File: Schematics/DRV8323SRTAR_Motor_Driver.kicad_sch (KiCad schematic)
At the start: 20 parts, among them U6 DRV8323SRTAR

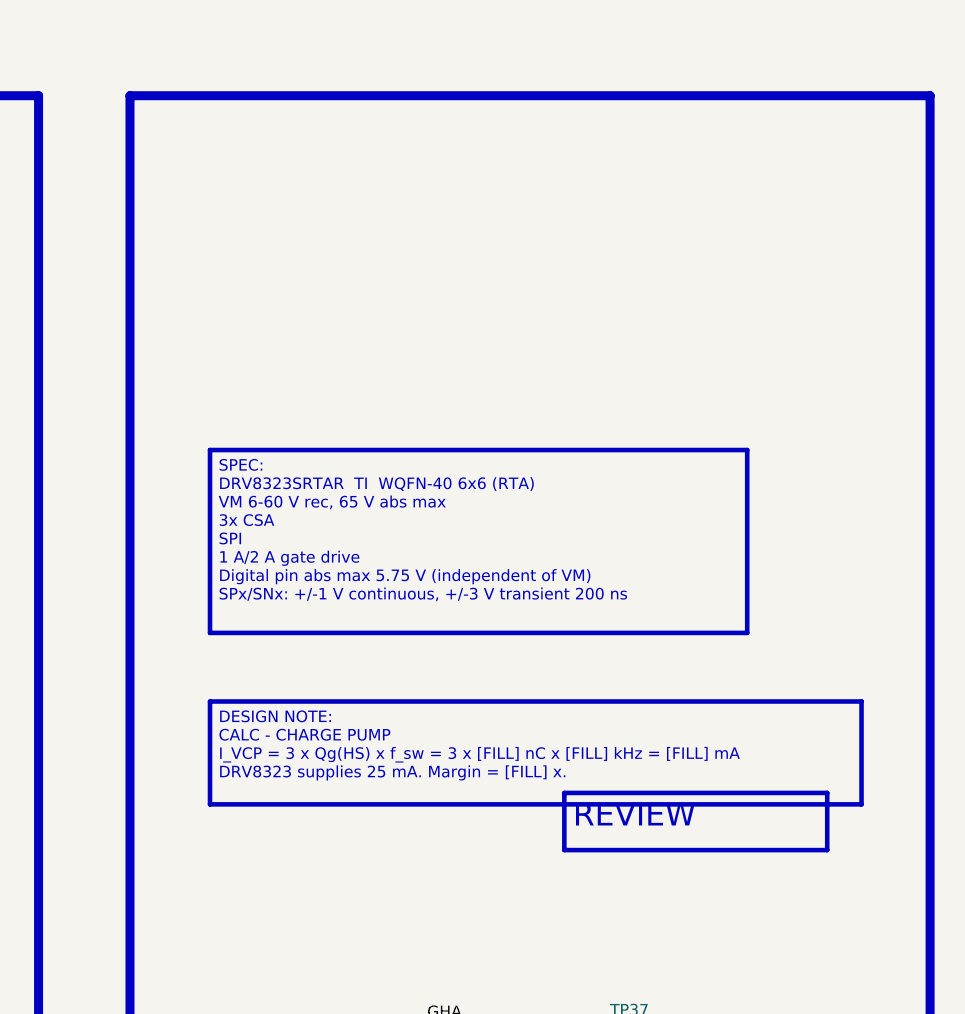
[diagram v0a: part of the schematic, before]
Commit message: Clean up schematic design notes; export schematic and PCB artwork PDFs
- Remove firmware-only notes (boot sequence, calibration procedure,
  firmware SPI/PWM settings) and template/empty text; keep hardware facts
- Tighten wording of all DESIGN/SPEC/ASSEMBLY/REV 1 notes and resize
  boxes so no note text wraps or overflows
- Re-export schematic PDF
- Add PCB artwork PDFs (combined and one per layer: silk, paste, mask,
  L1-L6 copper), board outline on every page

Co-Authored-By: Claude Opus 5.5 <noreply@anthropic.com>
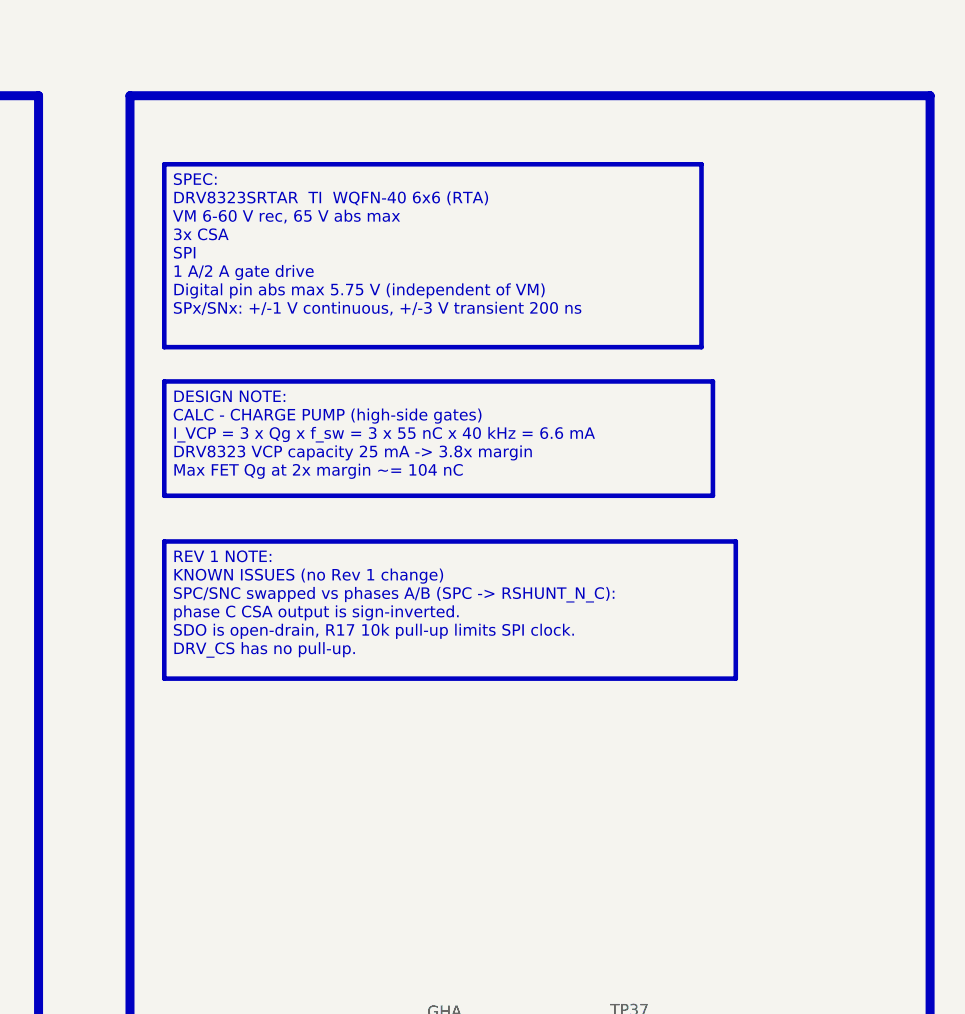
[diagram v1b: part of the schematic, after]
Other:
- company: (none) -> ${COMPANY}
- title: (none) -> Motor Control - Driver
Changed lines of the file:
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@@
 	(generator_version "10.0")
 	(paper "A3")
+	(title_block
+		(title "Motor Control - Driver")
+		(date "${RELEASE_DATE}")
+		(rev "${REVISION}")
+		(company "${COMPANY}")
+	)
 	(rectangle
 		(start 25.4 38.1)
@@
 		)
 	)
-	(text_box "REVIEW"
-		(exclude_from_sim no)
-		(at 350.52 115.57 0)
-		(size 29.21 6.35)
-		(margins 0.9525 0.9525 0.9525 0.9525)
-		(stroke
-			(width 0.508)
-			(type solid)
-			(color 255 0 0 1)
-		)
-		(fill
-			(type color)
-			(color 255 0 0 1)
-		)
-		(effects
-			(font
-				(size 2.54 2.54)
-				(color 0 0 0 1)
-			)
-			(justify left top)
-		)
-	)
 	(text_box "SPEC:\nDRV8323SRTAR  TI  WQFN-40 6x6 (RTA)\nVM 6-60 V rec, 65 V abs max \n3x CSA \nSPI\n1 A/2 A gate drive\nDigital pin abs max 5.75 V (independent of VM)\nSPx/SNx: +/-1 V continuous, +/-3 V transient 200 ns"
 		(exclude_from_sim no)
-		(at 311.15 77.4701 0)
+		(at 306.07 45.72 0)
 		(size 59.69 20.3199)
 		(margins 0.9525 0.9525 0.9525 0.9525)
@@
 		)
 	)
-	(text_box "DESIGN NOTE:\nCALC - CHARGE PUMP\nI_VCP = 3 x Qg(HS) x f_sw = 3 x [FILL] nC x [FILL] kHz = [FILL] mA\nDRV8323 supplies 25 mA. Margin = [FILL] x."
-		(exclude_from_sim no)
-		(at 311.15 105.4101 0)
-		(size 72.39 11.43)
-		(margins 0.9525 0.9525 0.9525 0.9525)
-		(stroke
-			(width 0.508)
-			(type solid)
-			(color 0 0 255 1)
-		)
-		(fill
-			(type color)
-			(color 255 255 255 1)
-		)
-		(effects
-			(font
-				(size 1.27 1.27)
-				(color 0 0 0 1)
-			)
-			(justify left top)
-		)
-	)
 	(text_box "Motor Driver\n"
 		(exclude_from_sim no)
@@
 		)
 	)
-)
+	(text_box "DESIGN NOTE:\nCALC - CHARGE PUMP (high-side gates)\nI_VCP = 3 x Qg x f_sw = 3 x 55 nC x 40 kHz = 6.6 mA\nDRV8323 VCP capacity 25 mA -> 3.8x margin\nMax FET Qg at 2x margin ~= 104 nC"
+		(exclude_from_sim no)
+		(at 306.07 69.85 0)
+		(size 60.96 12.70)
+		(margins 0.9525 0.9525 0.9525 0.9525)
+		(stroke
+			(width 0.508)
+			(type solid)
+			(color 0 0 255 1)
+		)
+		(fill
+			(type color)
+			(color 255 255 255 1)
+		)
+		(effects
+			(font
+				(size 1.27 1.27)
+				(color 0 0 0 1)
+			)
+			(justify left top)
+		)
+	)
+	(text_box "REV 1 NOTE:\nKNOWN ISSUES (no Rev 1 change)\nSPC/SNC swapped vs phases A/B (SPC -> RSHUNT_N_C):\n  phase C CSA output is sign-inverted.\nSDO is open-drain, R17 10k pull-up limits SPI clock.\nDRV_CS has no pull-up."
+		(exclude_from_sim no)
+		(at 306.07 87.63 0)
+		(size 63.5 15.24)
+		(margins 0.9525 0.9525 0.9525 0.9525)
+		(stroke
+			(width 0.508)
+			(type solid)
+			(color 255 0 0 1)
+		)
+		(fill
+			(type color)
+			(color 255 255 255 1)
+		)
+		(effects
+			(font
+				(size 1.27 1.27)
+				(color 0 0 0 1)
+			)
+			(justify left top)
+		)
+	))
